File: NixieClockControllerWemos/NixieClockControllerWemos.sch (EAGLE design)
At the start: 25 parts, among them IC1 NE555, Q1 BUZ11BV, T1 BC547

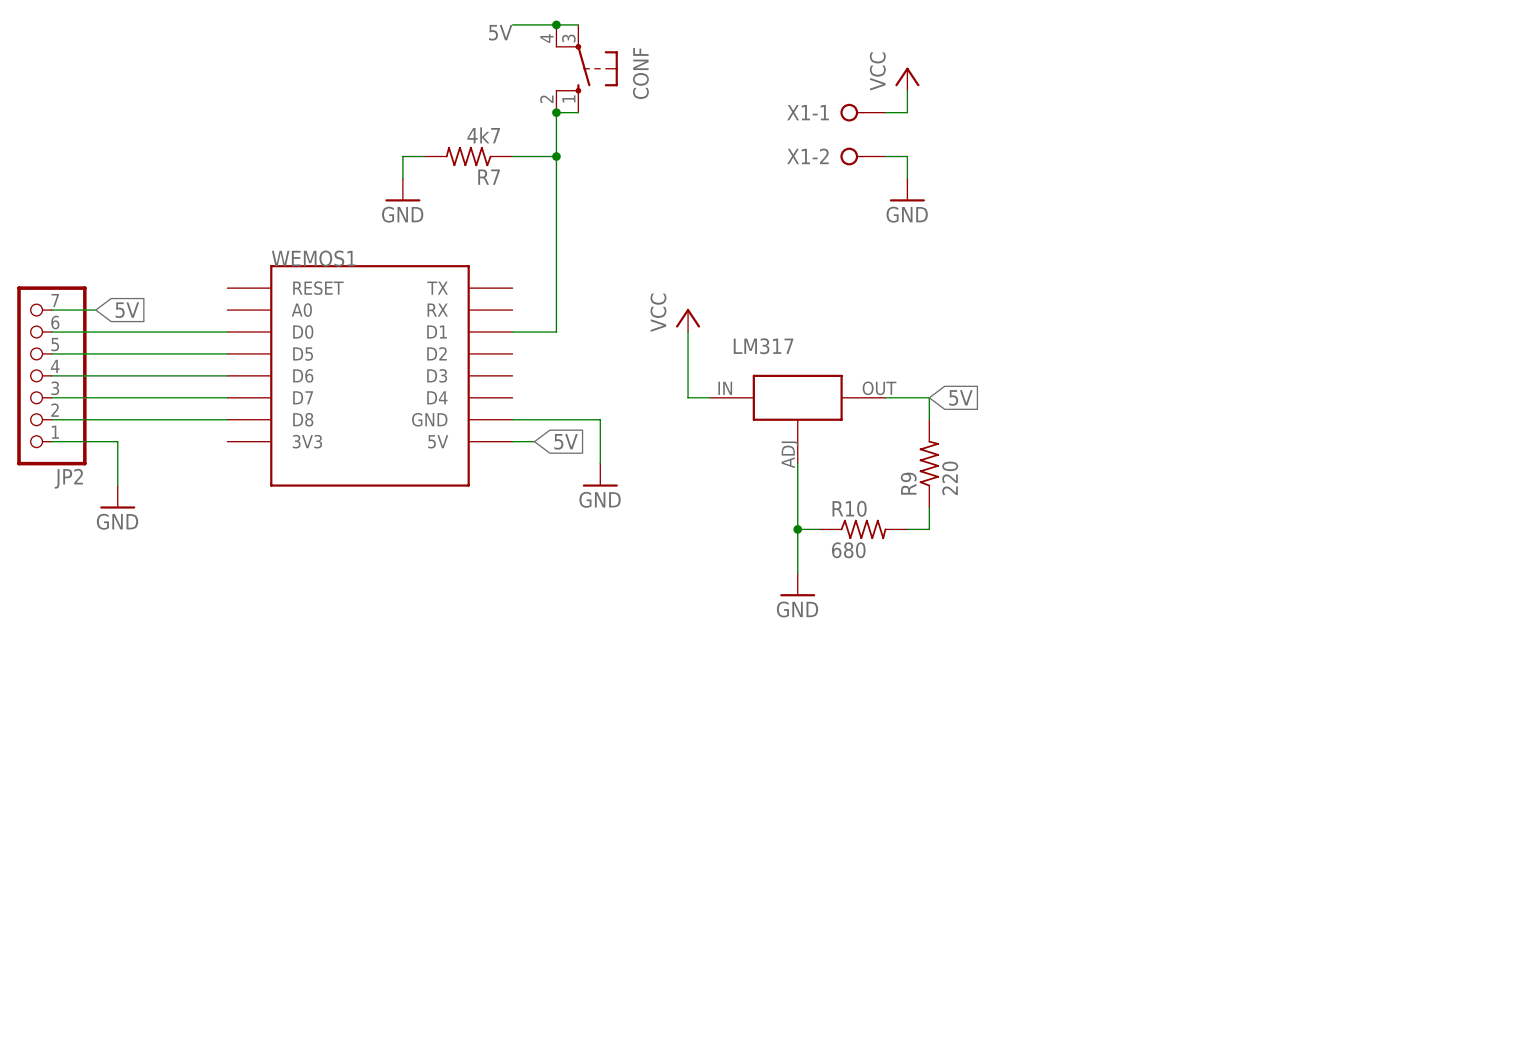
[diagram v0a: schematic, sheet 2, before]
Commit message: Fix LM317 wiring and add hex inverter.
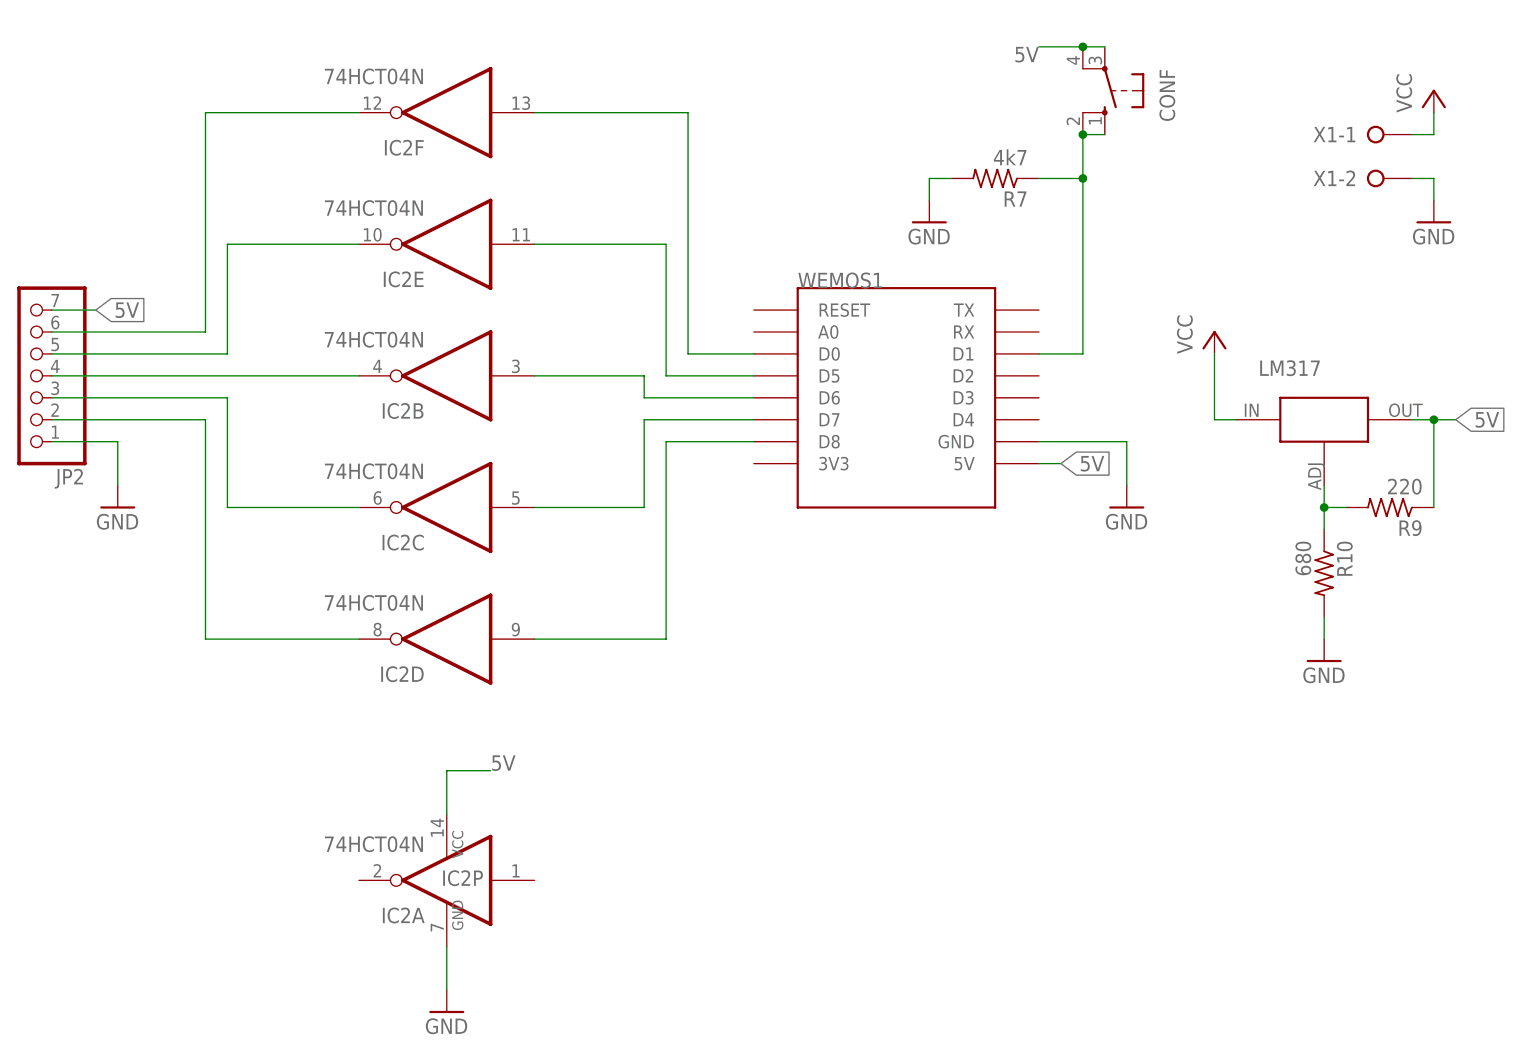
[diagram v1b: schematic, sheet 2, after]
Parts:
- added IC2: 74HCT04N, 74xx-eu:74HCT04N
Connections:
- new net N$17: IC2F.I, WEMOS1.D0
- new net N$18: IC2E.I, WEMOS1.D5
- new net N$19: IC2B.I, WEMOS1.D6
- new net N$20: IC2C.I, WEMOS1.D7
- new net N$21: IC2D.I, WEMOS1.D8
- net 5V: now also IC2P.VCC, R9.1; no longer R9.2
- net GND: now also IC2P.GND, R10.2; no longer R10.1, U$3.ADJ
- net N$11: now also IC2E.O; no longer WEMOS1.D5
- net N$12: now also R10.1, R9.2, U$3.ADJ; no longer R10.2, R9.1
- net N$13: now also IC2B.O; no longer WEMOS1.D6
- net N$14: now also IC2C.O; no longer WEMOS1.D7
- net N$15: now also IC2D.O; no longer WEMOS1.D8
- net N$5: now also IC2F.O; no longer WEMOS1.D0
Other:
- moved on the sheet: CONF, R10, R7, R9, WEMOS1, X1-1, X1-2
